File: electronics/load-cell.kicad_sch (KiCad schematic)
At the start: 15 parts, among them J1 Conn_01x03, J2 Conn_01x03, J3 Conn_01x03, J4 Conn_01x03, Q4 PNP, U1 HX711

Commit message: schematics
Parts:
- added C33, C34: 0.1u, Capacitor_SMD:C_0603_1608Metric, symbol Device:C
- added C36, C37: 1u, Capacitor_SMD:C_0603_1608Metric, symbol Device:C
- added U3: (no value), symbol MyScale:TXU0202
- added U7: TPS7A0533PDBV, Package_TO_SOT_SMD:SOT-23-5, symbol Regulator_Linear:TPS7A0533PDBV
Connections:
- net +3V3: now also C33.1, C37.1, U3.3 (VCCA), U7.5 (OUT)
- net Dout: now also U3.8 (B1Y); no longer U1.12 (DOUT)
- net GND: now also C33.2, C34.2, C36.2, C37.2, U3.2 (GND), U7.2 (GND)
- net Sck: now also U3.1 (B2); no longer U1.11 (PD_SCK)
- new net: U1.11 (PD_SCK), U3.4 (A2Y)
- new net: U1.12 (DOUT), U3.5 (A1)
- new net +1V8: C34.1, U3.7 (VCCB)
- new net Enable: U3.6 (OE), U7.3 (EN)
- new net VBAT: C36.1, U7.1 (IN)

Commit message: electronics: select footprints
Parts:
- U3: footprint (none) -> Package_SO:VSSOP-8_2.3x2mm_P0.5mm
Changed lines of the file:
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@@
 			)
 		)
-		(property "Footprint" ""
+		(property "Footprint" "Package_SO:VSSOP-8_2.3x2mm_P0.5mm"
 			(at 269.24 83.82 0)
 			(hide yes)

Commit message: electronics: initial placement
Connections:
- net +1V8: now also U3.3 (VCCA); no longer U3.7 (VCCB)
- net +3V3: now also U3.7 (VCCB); no longer U3.3 (VCCA)
- net Dout: now also U3.5 (A1); no longer U3.8 (B1Y)
- net Sck: now also U3.4 (A2Y); no longer U3.1 (B2)
- net at U1.11 (PD_SCK): now also U3.1 (B2); no longer U3.4 (A2Y)
- net at U1.12 (DOUT): now also U3.8 (B1Y); no longer U3.5 (A1)
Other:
- moved on the sheet: C34
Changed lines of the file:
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@@
 	)
 	(junction
-		(at 294.64 62.23)
+		(at 294.64 58.42)
 		(diameter 0)
 		(color 0 0 0 0)
@@
 	(wire
 		(pts
-			(xy 240.03 78.74) (xy 254 78.74)
+			(xy 298.45 78.74) (xy 284.48 78.74)
 		)
 		(stroke
@@
 	(wire
 		(pts
-			(xy 294.64 71.12) (xy 294.64 73.66)
+			(xy 294.64 67.31) (xy 294.64 69.85)
 		)
 		(stroke
@@
 	(wire
 		(pts
-			(xy 294.64 62.23) (xy 294.64 63.5)
+			(xy 294.64 58.42) (xy 294.64 59.69)
 		)
 		(stroke
@@
 	(wire
 		(pts
-			(xy 288.29 74.93) (xy 288.29 62.23)
+			(xy 288.29 74.93) (xy 288.29 58.42)
 		)
 		(stroke
@@
 	(wire
 		(pts
-			(xy 294.64 60.96) (xy 294.64 62.23)
+			(xy 294.64 57.15) (xy 294.64 58.42)
 		)
 		(stroke
@@
 	(wire
 		(pts
-			(xy 288.29 62.23) (xy 294.64 62.23)
+			(xy 288.29 58.42) (xy 294.64 58.42)
 		)
 		(stroke
@@
 	(hierarchical_label "Enable"
 		(shape input)
-		(at 240.03 78.74 180)
+		(at 298.45 78.74 0)
 		(effects
 			(font
 				(size 1.27 1.27)
 			)
-			(justify right)
+			(justify left)
 		)
 	)
@@
 	(symbol
 		(lib_id "Device:C")
-		(at 294.64 67.31 0)
+		(at 294.64 63.5 0)
 		(unit 1)
 		(body_style 1)
@@
 		(dnp no)
 		(property "Reference" "C34"
-			(at 298.45 66.0399 0)
+			(at 298.45 62.2299 0)
 			(show_name no)
 			(do_not_autoplace no)
@@
 		)
 		(property "Value" "0.1u"
-			(at 298.45 68.5799 0)
+			(at 298.45 64.7699 0)
 			(show_name no)
 			(do_not_autoplace no)
@@
 		)
 		(property "Footprint" "Capacitor_SMD:C_0603_1608Metric"
-			(at 295.6052 71.12 0)
+			(at 295.6052 67.31 0)
 			(hide yes)
 			(show_name no)
@@
 		)
 		(property "Datasheet" ""
-			(at 294.64 67.31 0)
+			(at 294.64 63.5 0)
 			(hide yes)
 			(show_name no)
@@
 		)
 		(property "Description" "Unpolarized capacitor"
-			(at 294.64 67.31 0)
+			(at 294.64 63.5 0)
 			(hide yes)
 			(show_name no)
@@
 	(symbol
 		(lib_id "power:+1V8")
-		(at 294.64 60.96 0)
+		(at 294.64 57.15 0)
 		(unit 1)
 		(body_style 1)
@@
 		(fields_autoplaced yes)
 		(property "Reference" "#PWR08"
-			(at 294.64 64.77 0)
+			(at 294.64 60.96 0)
 			(hide yes)
 			(show_name no)
@@
 		)
 		(property "Value" "+1V8"
-			(at 294.64 55.88 0)
+			(at 294.64 52.07 0)
 			(show_name no)
 			(do_not_autoplace no)
@@
 		)
 		(property "Footprint" ""
-			(at 294.64 60.96 0)
+			(at 294.64 57.15 0)
 			(hide yes)
 			(show_name no)
@@
 		)
 		(property "Datasheet" ""
-			(at 294.64 60.96 0)
+			(at 294.64 57.15 0)
 			(hide yes)
 			(show_name no)
@@
 		)
 		(property "Description" "Power symbol creates a global label with name \"+1V8\""
-			(at 294.64 60.96 0)
+			(at 294.64 57.15 0)
 			(hide yes)
 			(show_name no)
@@
 		(lib_id "MyScale:TXU0202")
 		(at 269.24 83.82 0)
+		(mirror y)
 		(unit 1)
 		(body_style 1)
@@
 		(in_pos_files yes)
 		(dnp no)
-		(fields_autoplaced yes)
 		(property "Reference" "U3"
 			(at 269.24 68.58 0)
@@
 	(symbol
 		(lib_id "power:GND")
-		(at 294.64 73.66 0)
+		(at 294.64 69.85 0)
 		(mirror y)
 		(unit 1)
@@
 		(in_pos_files yes)
 		(dnp no)
-		(fields_autoplaced yes)
 		(property "Reference" "#PWR061"
-			(at 294.64 80.01 0)
+			(at 294.64 76.2 0)
 			(hide yes)
 			(show_name no)
@@
 		)
 		(property "Value" "GND"
-			(at 294.64 78.74 0)
+			(at 294.64 73.914 0)
 			(show_name no)
 			(do_not_autoplace no)
@@
 		)
 		(property "Footprint" ""
-			(at 294.64 73.66 0)
+			(at 294.64 69.85 0)
 			(hide yes)
 			(show_name no)
@@
 		)
 		(property "Datasheet" ""
-			(at 294.64 73.66 0)
+			(at 294.64 69.85 0)
 			(hide yes)
 			(show_name no)
@@
 		)
 		(property "Description" "Power symbol creates a global label with name \"GND\" , ground"
-			(at 294.64 73.66 0)
+			(at 294.64 69.85 0)
 			(hide yes)
 			(show_name no)

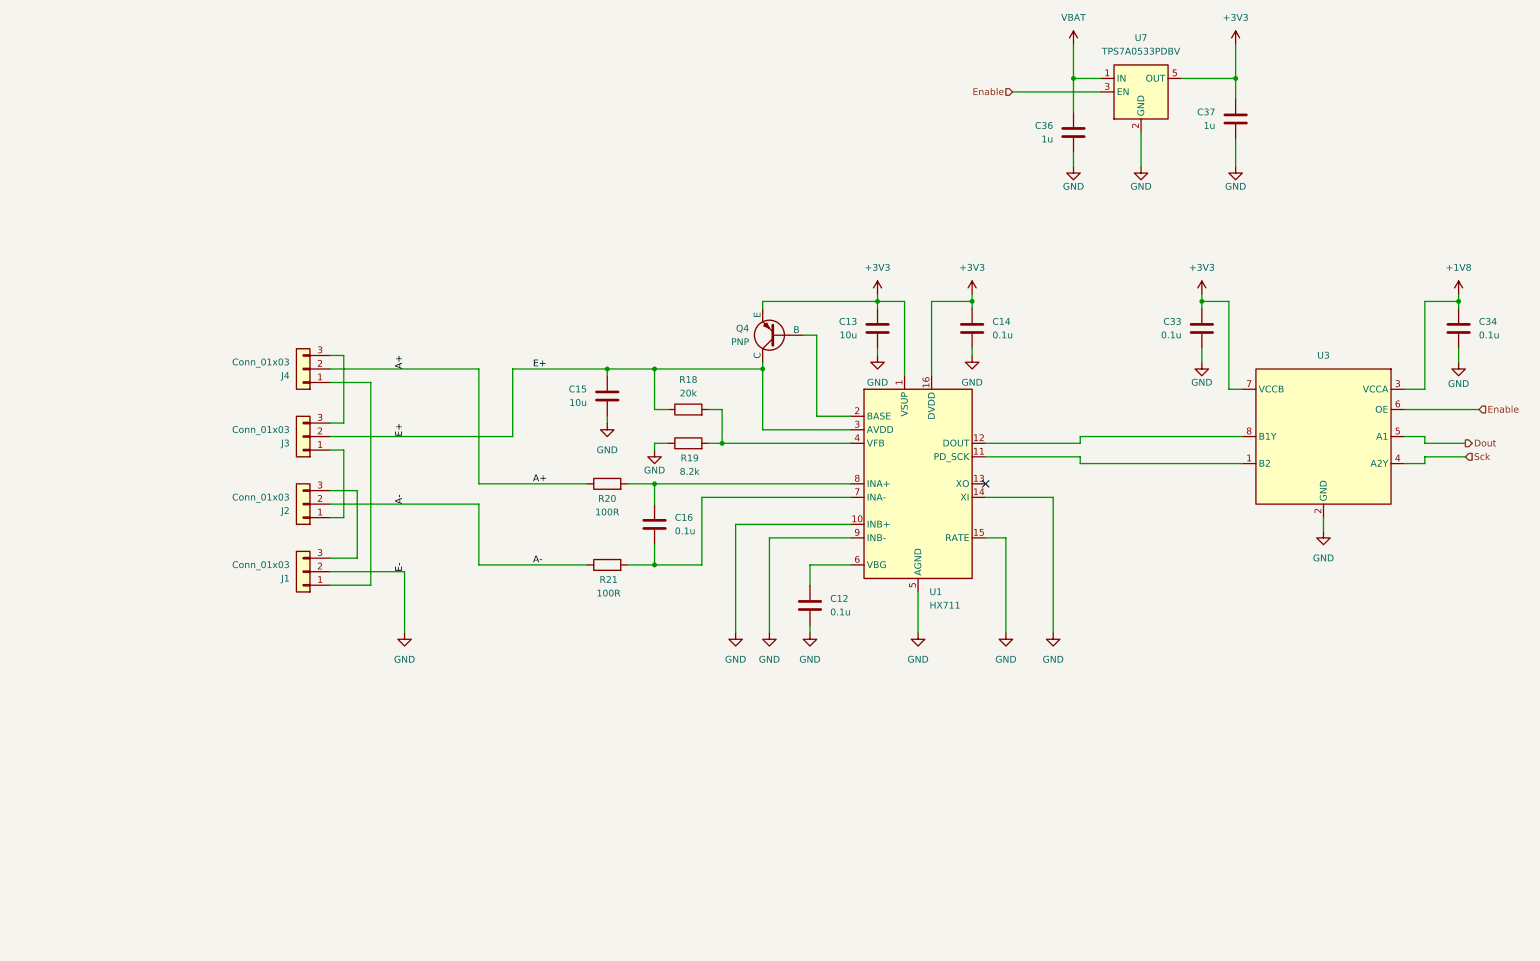
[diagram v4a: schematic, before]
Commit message: electronics: replace A7670 footprint
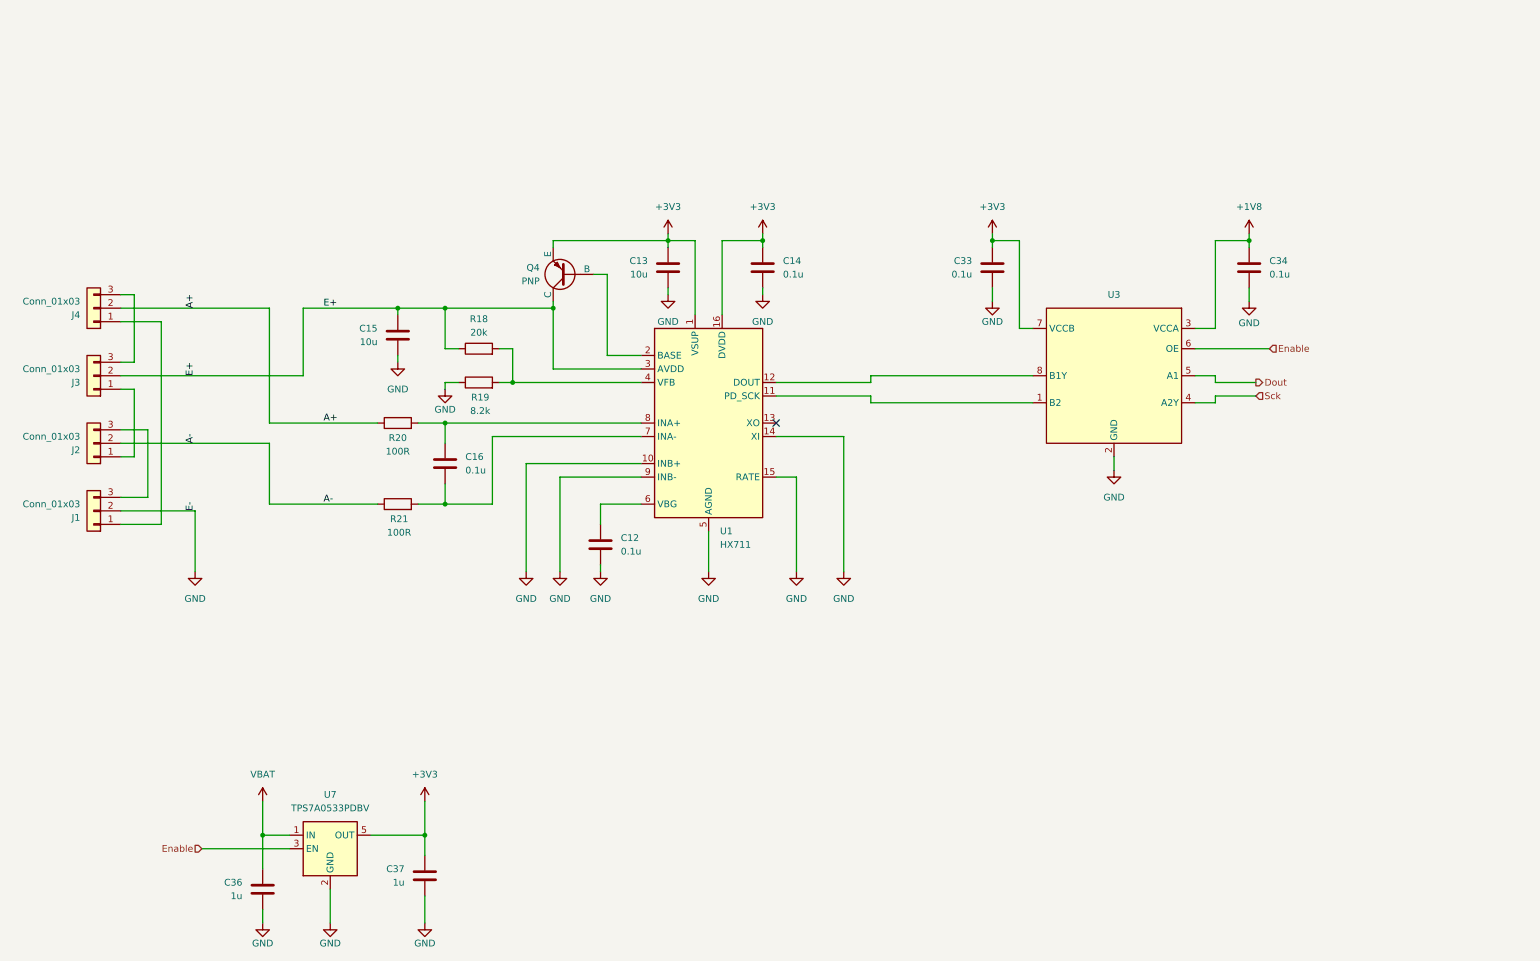
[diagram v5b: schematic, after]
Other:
- moved on the sheet: C12, C13, C14, C15, C16, C33, C34, C36, C37, J1, J2, J3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

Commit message: electronics: final touches
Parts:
- U3: value (none) -> TXU0202; MPN (none) -> TXU0202
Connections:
- net Dout: now also U3.4 (A2Y); no longer U3.5 (A1)
- net Sck: now also U3.5 (A1); no longer U3.4 (A2Y)
- net at U3.1 (B2): now also U1.12 (DOUT); no longer U1.11 (PD_SCK)
- net at U3.8 (B1Y): now also U1.11 (PD_SCK); no longer U1.12 (DOUT)
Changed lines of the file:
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@@
 	(wire
 		(pts
-			(xy 248.92 73.66) (xy 248.92 72.39)
+			(xy 245.11 72.39) (xy 250.19 72.39)
 		)
 		(stroke
@@
 	(wire
 		(pts
-			(xy 229.87 87.63) (xy 229.87 90.17)
+			(xy 194.31 77.47) (xy 214.63 77.47)
 		)
 		(stroke
@@
 	(wire
 		(pts
-			(xy 184.15 77.47) (xy 214.63 77.47)
+			(xy 229.87 87.63) (xy 229.87 90.17)
 		)
 		(stroke
@@
 	(wire
 		(pts
+			(xy 194.31 73.66) (xy 194.31 77.47)
+		)
+		(stroke
+			(width 0)
+			(type default)
+		)
+	)
+	(wire
+		(pts
 			(xy 43.18 97.79) (xy 57.15 97.79)
 		)
@@
 	(wire
 		(pts
-			(xy 256.54 73.66) (xy 248.92 73.66)
-		)
-		(stroke
-			(width 0)
-			(type default)
-		)
-	)
-	(wire
-		(pts
 			(xy 124.46 59.69) (xy 124.46 58.42)
 		)
@@
 	(wire
 		(pts
-			(xy 245.11 77.47) (xy 248.92 77.47)
-		)
-		(stroke
-			(width 0)
-			(type default)
-		)
-	)
-	(wire
-		(pts
 			(xy 212.09 63.5) (xy 212.09 46.99)
 		)
@@
 	(wire
 		(pts
-			(xy 248.92 76.2) (xy 248.92 77.47)
-		)
-		(stroke
-			(width 0)
-			(type default)
-		)
-	)
-	(wire
-		(pts
 			(xy 104.14 74.93) (xy 104.14 73.66)
 		)
@@
 	(wire
 		(pts
-			(xy 104.14 92.71) (xy 104.14 96.52)
+			(xy 196.85 72.39) (xy 214.63 72.39)
 		)
 		(stroke
@@
 	(wire
 		(pts
-			(xy 166.37 73.66) (xy 184.15 73.66)
+			(xy 104.14 92.71) (xy 104.14 96.52)
 		)
 		(stroke
@@
 	(wire
 		(pts
-			(xy 245.11 63.5) (xy 248.92 63.5)
+			(xy 166.37 73.66) (xy 194.31 73.66)
 		)
 		(stroke
@@
 	(wire
 		(pts
-			(xy 50.8 62.23) (xy 43.18 62.23)
+			(xy 245.11 63.5) (xy 248.92 63.5)
 		)
 		(stroke
@@
 	(wire
 		(pts
-			(xy 48.26 82.55) (xy 48.26 95.25)
+			(xy 50.8 62.23) (xy 43.18 62.23)
 		)
 		(stroke
@@
 	(wire
 		(pts
-			(xy 71.12 96.52) (xy 91.44 96.52)
+			(xy 48.26 82.55) (xy 48.26 95.25)
 		)
 		(stroke
@@
 	(wire
 		(pts
-			(xy 184.15 72.39) (xy 214.63 72.39)
+			(xy 71.12 96.52) (xy 91.44 96.52)
 		)
 		(stroke
@@
 	(wire
 		(pts
-			(xy 245.11 72.39) (xy 248.92 72.39)
-		)
-		(stroke
-			(width 0)
-			(type default)
-		)
-	)
-	(wire
-		(pts
 			(xy 207.01 45.72) (xy 207.01 46.99)
 		)
@@
 	(wire
 		(pts
-			(xy 166.37 76.2) (xy 184.15 76.2)
+			(xy 166.37 76.2) (xy 196.85 76.2)
 		)
 		(stroke
@@
 	(wire
 		(pts
-			(xy 256.54 76.2) (xy 248.92 76.2)
+			(xy 45.72 57.15) (xy 45.72 69.85)
 		)
 		(stroke
@@
 	(wire
 		(pts
-			(xy 184.15 73.66) (xy 184.15 72.39)
+			(xy 82.55 168.91) (xy 82.55 175.26)
 		)
 		(stroke
@@
 	(wire
 		(pts
-			(xy 45.72 57.15) (xy 45.72 69.85)
+			(xy 119.38 109.22) (xy 119.38 88.9)
 		)
 		(stroke
@@
 	(wire
 		(pts
-			(xy 82.55 168.91) (xy 82.55 175.26)
+			(xy 170.18 91.44) (xy 170.18 109.22)
 		)
 		(stroke
@@
 	(wire
 		(pts
-			(xy 119.38 109.22) (xy 119.38 88.9)
+			(xy 48.26 95.25) (xy 43.18 95.25)
 		)
 		(stroke
@@
 	(wire
 		(pts
-			(xy 170.18 91.44) (xy 170.18 109.22)
+			(xy 245.11 77.47) (xy 250.19 77.47)
 		)
 		(stroke
@@
 	(wire
 		(pts
-			(xy 48.26 95.25) (xy 43.18 95.25)
+			(xy 57.15 97.79) (xy 57.15 109.22)
 		)
 		(stroke
@@
 	(wire
 		(pts
-			(xy 57.15 97.79) (xy 57.15 109.22)
+			(xy 100.33 152.4) (xy 100.33 158.75)
 		)
 		(stroke
@@
 	(wire
 		(pts
-			(xy 100.33 152.4) (xy 100.33 158.75)
+			(xy 196.85 76.2) (xy 196.85 72.39)
 		)
 		(stroke
@@
 	(wire
 		(pts
-			(xy 184.15 76.2) (xy 184.15 77.47)
-		)
-		(stroke
-			(width 0)
-			(type default)
-		)
-	)
-	(wire
-		(pts
 			(xy 153.67 101.6) (xy 153.67 109.22)
 		)
@@
 	(hierarchical_label "Dout"
 		(shape output)
-		(at 256.54 73.66 0)
+		(at 250.19 77.47 0)
 		(effects
 			(font
@@
 	(hierarchical_label "Sck"
 		(shape input)
-		(at 256.54 76.2 0)
+		(at 250.19 72.39 0)
 		(effects
 			(font
@@
 			)
 		)
-		(property "Value" ""
-			(at 229.87 72.39 0)
+		(property "Value" "TXU0202"
+			(at 239.776 88.392 0)
 			(show_name no)
 			(do_not_autoplace no)
@@
 			(at 229.87 72.39 0)
 			(hide yes)
+			(show_name no)
+			(do_not_autoplace no)
+			(effects
+				(font
+					(size 1.27 1.27)
+				)
+			)
+		)
+		(property "MPN" "TXU0202"
+			(at 229.87 72.39 0)
+			(hide yes)

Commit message: electronics: add MPNs
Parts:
- U3: MPN TXU0202 -> TXU0202DCUR
- U7: MPN (none) -> TPS7A0533PDBV
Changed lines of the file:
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@@
+			)
+		)
+		(property "MPN" "TPS7A0533PDBV"
+			(at 82.55 161.29 0)
+			(hide yes)
+			(show_name no)
+			(do_not_autoplace no)
+			(effects
+				(font
+					(size 1.27 1.27)
+				)
 			)
 		)
@@
 			)
 		)
-		(property "MPN" "TXU0202"
+		(property "MPN" "TXU0202DCUR"
 			(at 229.87 72.39 0)
 			(hide yes)

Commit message: electronics: simplify BOM and fix issues
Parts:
- C13, C15: footprint Capacitor_SMD:C_0603_1608Metric -> Capacitor_SMD:C_0805_2012Metric
- J1, J2, J3, J4: now left out of the parts list
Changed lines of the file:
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@@
 			)
 		)
-		(property "Footprint" "Capacitor_SMD:C_0603_1608Metric"
+		(property "Footprint" "Capacitor_SMD:C_0805_2012Metric"
 			(at 94.2848 68.58 0)
 			(hide yes)
@@
 		(body_style 1)
 		(exclude_from_sim no)
-		(in_bom yes)
-		(on_board yes)
-		(in_pos_files yes)
+		(in_bom no)
+		(on_board yes)
+		(in_pos_files no)
 		(dnp no)
 		(fields_autoplaced yes)
@@
 		(body_style 1)
 		(exclude_from_sim no)
-		(in_bom yes)
-		(on_board yes)
-		(in_pos_files yes)
+		(in_bom no)
+		(on_board yes)
+		(in_pos_files no)
 		(dnp no)
 		(fields_autoplaced yes)
@@
 		(body_style 1)
 		(exclude_from_sim no)
-		(in_bom yes)
-		(on_board yes)
-		(in_pos_files yes)
+		(in_bom no)
+		(on_board yes)
+		(in_pos_files no)
 		(dnp no)
 		(fields_autoplaced yes)
@@
 		(body_style 1)
 		(exclude_from_sim no)
-		(in_bom yes)
-		(on_board yes)
-		(in_pos_files yes)
+		(in_bom no)
+		(on_board yes)
+		(in_pos_files no)
 		(dnp no)
 		(fields_autoplaced yes)
@@
 			)
 		)
-		(property "Footprint" "Capacitor_SMD:C_0603_1608Metric"
+		(property "Footprint" "Capacitor_SMD:C_0805_2012Metric"
 			(at 145.0848 55.88 0)
 			(hide yes)
